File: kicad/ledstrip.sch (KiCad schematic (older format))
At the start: 41 parts, among them J1 Molex USB mini B 0548190519, J2 Conn_02x06_Top_Bottom, U1 MCP2221A-I_SL, U2 PCA9955TW, U3 PCA9955TW, U4 SN74LS07N, U5 PCA9617A

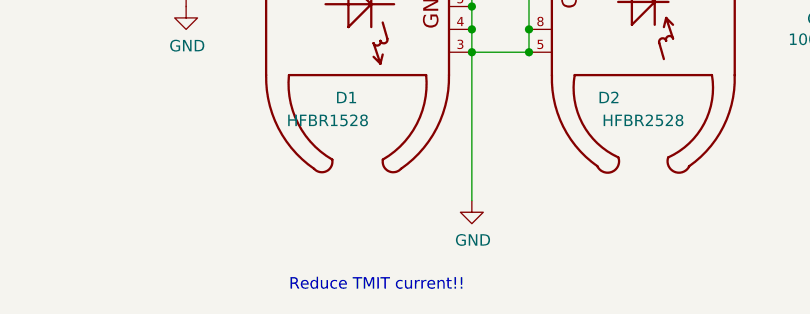
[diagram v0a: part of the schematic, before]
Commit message: Redrew HFBR component graphics (had rendered badly in PDF)
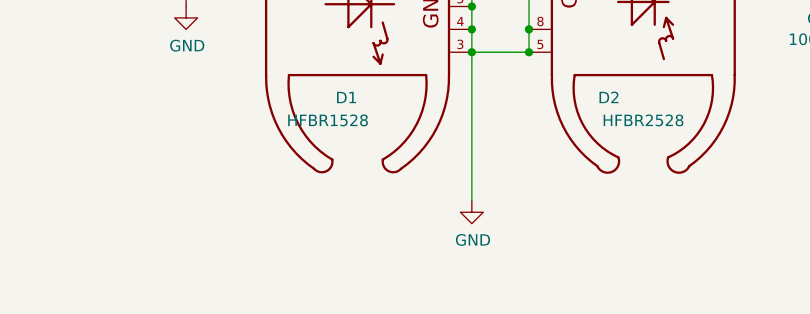
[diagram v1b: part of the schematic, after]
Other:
- note removed: "Reduce TMIT current!!\n"
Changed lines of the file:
@@
 EESchema Schematic File Version 4
-LIBS:ledstrip-cache
-EELAYER 26 0
+EELAYER 30 0
 EELAYER END
 $Descr A4 11693 8268
@@
 Rev "1.0"
 Comp "PSI"
-Comment1 ""
+Comment1 "Till Straumann, 10/2020"
 Comment2 ""
 Comment3 ""
@@
 	1    0    0    -1
 $EndComp
-Text Notes 4200 7600 0    50   ~ 0
-Reduce TMIT current!!\n
 Wire Wire Line
 	5250 6250 5250 6450

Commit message: ledstrip.sch: added some comments
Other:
- note added: "I2C can be controlled via:\n - optical link (active low: light = logical low)\n - USB (usb-i2c bridge)\n - PMOD connector (fpga development board)\n I/O voltage from 0.5 - 5.5V\nPower is always supplied from USB connector."
- note added: "I2C-Controlled LED Bar-Graph"
- note added: "PMOD Connector\n(e.g., for testing with Zynq development board)"
- note added: "SCL Optical I/O"
- note added: "SDA Optical I/O"
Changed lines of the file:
@@
 	0    -1   -1   0
 $EndComp
-Wire Wire Line
-	8350 5400 8350 5500
 Connection ~ 8350 5500
 Wire Wire Line
@@
 L power:GND #PWR09
 U 1 1 5FA4EA4E
-P 8350 6300
-F 0 "#PWR09" H 8350 6050 50  0001 C CNN
-F 1 "GND" H 8355 6127 50  0000 C CNN
-F 2 "" H 8350 6300 50  0001 C CNN
-F 3 "" H 8350 6300 50  0001 C CNN
-	1    8350 6300
+P 8350 6050
+F 0 "#PWR09" H 8350 5800 50  0001 C CNN
+F 1 "GND" H 8355 5877 50  0000 C CNN
+F 2 "" H 8350 6050 50  0001 C CNN
+F 3 "" H 8350 6050 50  0001 C CNN
+	1    8350 6050
 	-1   0    0    -1
 $EndComp
@@
 	6650 6150 6650 6250
 Wire Wire Line
-	8350 5700 8350 6300
-Wire Wire Line
 	5000 6550 5000 7200
 $Comp
@@
 Text Notes 900  3350 0    50   ~ 0
 NOTE:\nFootprint swapped!\nMount from bottom side of PCB!
+Text Notes 7950 6450 0    50   ~ 0
+SDA Optical I/O
+Text Notes 4750 7650 0    50   ~ 0
+SCL Optical I/O
+Wire Wire Line
+	8350 5700 8350 6050
+Text Notes 1550 7350 0    50   ~ 0
+PMOD Connector\n(e.g., for testing with Zynq development board)
+Wire Notes Line style solid rgb(255, 0, 0)
+	850  3050 850  3400
+Wire Notes Line style solid rgb(255, 0, 0)
+	850  3400 2200 3400
+Wire Notes Line style solid rgb(255, 0, 0)
+	2200 3400 2200 3050
+Wire Notes Line style solid rgb(255, 0, 0)
+	2200 3050 850  3050
+Wire Wire Line
+	8350 5450 8350 5500
+Wire Wire Line
+	8350 5400 8350 5500
+Text Notes 850  750  0    118  Italic 0
+I2C-Controlled LED Bar-Graph
+Text Notes 850  1300 0    50   ~ 0
+I2C can be controlled via:\n - optical link (active low: light = logical low)\n - USB (usb-i2c bridge)\n - PMOD connector (fpga development board)\n    I/O voltage from 0.5 - 5.5V\nPower is always supplied from USB connector.
 $EndSCHEMATC
